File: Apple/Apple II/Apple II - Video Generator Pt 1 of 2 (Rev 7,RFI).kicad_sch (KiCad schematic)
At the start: 0 parts

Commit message: Finished Apple II - Sheet 16 - Video Generator Part 1 (Rev 7, RFI)
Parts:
- added A?: 74166, symbol Apple II:A3_74166
- added A?: 74LS151, symbol Apple II:A9_74LS151
- added A? (x2): 74LS02, symbol Apple II:A12_74LS02
- added A?, a?: 74LS74, symbol Apple II:A11_74LS74
- added A?: 74LS194, symbol Apple II:A10_74LS194
- added B11, B?: 74LS08, symbol Apple II:B11_74LS08
- added B? (x2): 74LS02, symbol Apple II:B13_74LS02
- added B?: 74LS74, symbol Apple II:B10_74LS74
- added B?: 74LS194, symbol Apple II:B9_74LS194
- added B?: 74LS11, symbol Apple II:B12_74LS11
- added B?: 74S86, symbol Apple II:B2_74S86
- added B?: 74LS194, symbol Apple II:B4_74LS194
- added C?: 0.1µF, symbol Device:C_Small
- added JP10: 10, symbol Apple II:Bowtie_SolderJumper
- added JP11: 11, symbol Apple II:Bowtie_SolderJumper
- added JP5: 5, symbol Apple II:Bowtie_SolderJumper
- added JP9: 9, symbol Apple II:Bowtie_SolderJumper
- added N1, N?: 1, symbol Apple II:NOTE_NUMBER
- added N?: NOTE_SHEET16_CHARPROM, symbol Apple II:NOTE_SHEET16_CHARPROM
- added R?: 12K, symbol Device:R_US
- added R?: 3.3M, symbol Device:R_US
- added TP4: TestPoint, symbol Connector:TestPoint
- added U?: A5_2316B, symbol Apple II:A5_2316B
- added U? (x2): B8_74LS174, symbol Apple II:B8_74LS174
- added U?: B3_555, Package_SO:SOIC-8_3.9x4.9mm_P1.27mm, symbol Apple II:B3_555
- added U?: B5_74LS174, symbol Apple II:B5_74LS174
- added U?: A8_74LS257, symbol Apple II:A8_74LS257
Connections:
- new net: B?.13, TP4.1, U?.3 (D0)
- new net: A?.2 (A), A?.6 (D3), B?.4
- new net: B?.11, B?.5
- new net: R?.1, R?.2, U?.7 (DIS)
- new net: A?.4 (C), U?.10 (O2)
- new net: A?.5 (D), U?.11 (O3)
- new net: A?.10 (E), U?.13 (O4)
- new net: A?.11 (F), U?.14 (O5)
- new net: A?.12 (G), U?.15 (O6)
- new net: A?.14 (H), U?.16 (O7)
- new net: JP11.2 (B), U?.17 (O8)
- new net: A?.3 (B), U?.9 (O1)
- new net: U?.14 (D4), U?.2 (Q0), U?.6 (1B)
- new net: U?.15 (Q5), U?.3 (D0)
- new net: C?.2, R?.1, U?.2 (TR), U?.6 (TH)
- new net: A?.1 (SER.IN), A?.12 (Q3), B?.12
- new net: A?.13 (Q_{H}), B?.13
- new net: A?.9 (~{CLR}), JP5.1 (A)
- new net: A?.1 (D3), a?.9 (Q)
- new net: A?.10 (B), A?.15 (Q0)
- new net: A?.11 (A), A?.14 (Q1)
- new net: A?.12 (D7), B?.13 (Q2)
- new net: A?.13 (D6), B?.15 (Q0), B?.7 (DSL), U?.3 (1A)
- new net: A?.14 (D5), B?.13 (Q2)
- new net: A?.15 (D4), A?.2 (D2)
- new net: A?.3 (D1), A?.4 (D0), B?.11
- new net: A?.5 (Y), B?.2 (D)
- new net: A?.13 (Q2), A?.7 (~{ST})
- new net: A?.1 (~{CLR}), A?.13, A?.9 (C)
- new net: B?.11, B?.6
- new net: B?.13, U?.3 (OUT)
- new net: A?.10, A?.11
- new net: B?.10 (S1), B?.10 (S1)
- new net: B?.11, B?.11
- new net: B?.9 (S0), B?.9 (S0)
- new net: A?.6 (~{Q}), U?.1 (S)
- new net: A?.4 (D1), U?.12 (ZD)
- new net: B?.15 (Q0), U?.2 (0A), a?.12 (D)
- new net: B?.7 (DSL), U?.4 (ZA)
- new net: A?.3 (D0), U?.7 (ZB)
- new net: B?.10 (S1), U?.9 (ZC)
- new net: B?.12, JP11.1 (A)
- new net +5V: R?.2, U?.21 (CS3), U?.4 (~{R}), U?.8 (VCC)
- new net 14M: A?.11 (Cp), A?.7 (CL2), B?.11, B?.3 (CLK), a?.11 (CLK)
- new net 7M_{36}: A?.6 (CL1)
- new net B8_{2}: A?.8, A?.9, B11.5, U?.2 (Q0)
- new net BLANKING: A?.5 (D2)
- new net DL0: B?.3 (D0), U?.5 (A3)
- new net DL1: B?.4 (D1), U?.4 (A4)
- new net DL2: B?.5 (D2), U?.3 (A5)
- new net DL3: B?.6 (D3), U?.2 (A6)
- new net DL4: B?.3 (D0), U?.1 (A7)
- new net DL5: B?.4 (D1), U?.23 (A8)
- new net DL6: B?.5 (D2), JP10.1 (A), JP10.2 (B), U?.22 (A9)
- new net DL7: B?.6, B?.6 (D3), JP9.1 (A), JP9.2 (B), U?.13 (1D), U?.19 (A10)
- new net Earth: A?.4 (~{P}), C?.1, U?.1 (GND), U?.15 (~{E}), U?.18 (~{CS2}), U?.20 (~{CS1})
- new net H0: U?.14 (0D)
- new net HIRES: B11.6
- new net HIRES MODE: A?.12, B11.4
- new net LD194: A?.10 (S1), A?.9 (S0), B?.9 (S0)
- new net MIX MODE: B?.5
- new net SOFT 5: A?.2 (D), A?.3 (CLK), B?.1 (~{CLR}), B?.4 (~{P}), JP5.2 (B), U?.1 (~{CLR}), U?.1 (~{CLR}), U?.1 (~{CLR}), U?.11 (0C), a?.10 (~{P}), a?.13 (~{CLR})
- new net TEXT MODE: B?.12
- new net V2: B?.3
- new net V4: B?.4
- new net VA: U?.8 (A0)
- new net VB: U?.7 (A1)
- new net VC: U?.5 (0B), U?.6 (A2)
- new net VIDEO_DATA: B?.5 (Q)
- new net ~{7M}: U?.10 (1C)
- new net ~{LDPS}: A?.15 (~{LD})
- new net ~{RAS}: U?.9 (Cp), U?.9 (Cp), U?.9 (Cp)
- no-connect marks 0 -> 3
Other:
- note added: "BOWTIE 5 PROVIDED ON REV. 7 ONLY"
- note added: "FROM CLOCK GENERATOR"
- note added: "FROM ON-BOARD I/O"
- note added: "FROM PART 2"
- note added: "FROM RAM"
- note added: "FROM VIDEO ADDRESS GENERATOR"
- note added: "TO MEMORY ADDRESS"
- note added: "TO PART 2"
- note added: "TO PERIPHERAL I/O"
- title: (none) -> Apple II - Video Generator Part 1

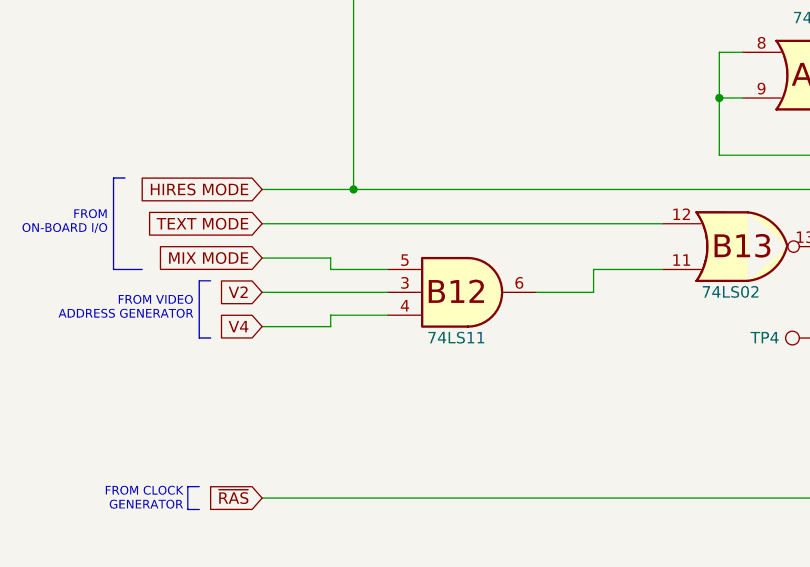
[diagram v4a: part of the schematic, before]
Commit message: Finished Apple II - Single Piece Keyboard
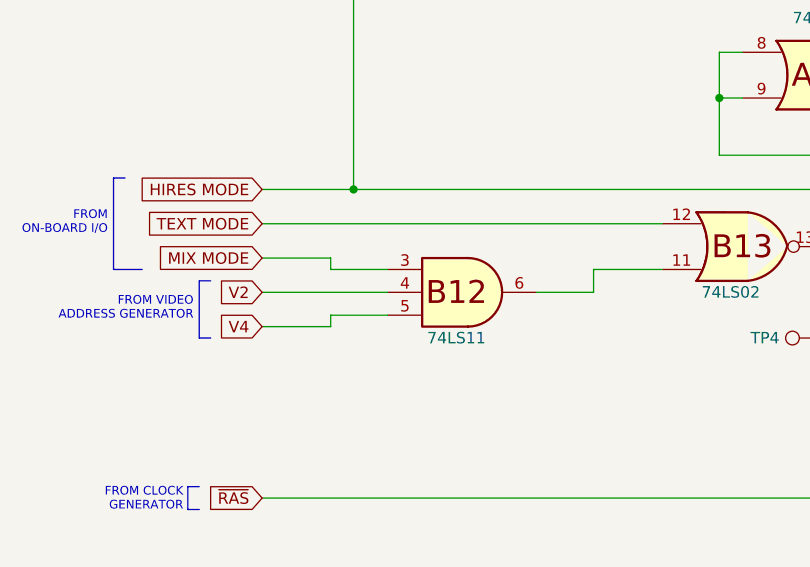
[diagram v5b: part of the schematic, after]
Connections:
- net MIX MODE: now also B?.3; no longer B?.5
- net V2: now also B?.4; no longer B?.3
- net V4: now also B?.5; no longer B?.4
